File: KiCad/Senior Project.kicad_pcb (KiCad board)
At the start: 4 copper layers, 59.2 x 89.2 mm, 46 parts, among them J2 Screw_Terminal_01x02, J3 Screw_Terminal_01x06, J4 Conn_ARM_JTAG_SWD_10, J5 Conn_01x03, J6 Conn_01x02, J7 USB4105-GF-A, Q2 IRLML0030, Q3 IRLML0030, Q4 IRLML0030, SW1 SW_Push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

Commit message: all DRC error fixed other than hole clearence issue, Only radio connection left to route
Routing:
- net GND: track 34.4 -> 7.33 mm, vias 4 -> 10
- net +3V3: track 216.8 -> 222.3 mm
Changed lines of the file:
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@@
-	)
-	(segment
-		(start 166.2 124.9)
-		(end 169 122.1)
-		(width 0.2)
-		(layer "F.Cu")
-		(net 1)
 	)
 	(segment
@@
 	)
 	(segment
-		(start 169 135.3)
-		(end 166.2 132.5)
-		(width 0.2)
-		(layer "F.Cu")
-		(net 1)
-	)
-	(segment
-		(start 166.2 125.125)
-		(end 163.945 125.125)
-		(width 0.2)
-		(layer "F.Cu")
-		(net 1)
-	)
-	(segment
 		(start 174.7 135.3)
 		(end 176.6 135.3)
@@
 	)
 	(segment
-		(start 156.860589 109.258217)
-		(end 155.284653 107.682281)
-		(width 0.2)
-		(layer "F.Cu")
-		(net 1)
-	)
-	(segment
 		(start 140.5 93.2)
 		(end 140.5 92.7)
@@
 		(start 163.945 125.125)
 		(end 163.6 125.47)
-		(width 0.2)
-		(layer "F.Cu")
-		(net 1)
-	)
-	(segment
-		(start 179.4 124.9)
-		(end 176.6 122.1)
 		(width 0.2)
 		(layer "F.Cu")
@@
 	)
 	(segment
-		(start 179.4 132.5)
-		(end 176.6 135.3)
-		(width 0.2)
-		(layer "F.Cu")
-		(net 1)
-	)
-	(segment
 		(start 145.7 123.545)
 		(end 145.7 122.9)
@@
 	)
 	(segment
-		(start 160.260589 111.339411)
-		(end 157.860589 111.339411)
-		(width 0.2)
-		(layer "F.Cu")
-		(net 1)
-	)
-	(segment
 		(start 147.6 123.4)
 		(end 147.8413 123.4)
@@
 	)
 	(segment
-		(start 156.860589 110.239411)
-		(end 156.860589 109.258217)
-		(width 0.2)
-		(layer "F.Cu")
-		(net 1)
-	)
-	(segment
 		(start 147.455 123.545)
 		(end 147.6 123.4)
-		(width 0.2)
-		(layer "F.Cu")
-		(net 1)
-	)
-	(segment
-		(start 159.460589 109.939411)
-		(end 160.560589 111.039411)
-		(width 0.2)
-		(layer "F.Cu")
-		(net 1)
-	)
-	(segment
-		(start 157.860589 111.239411)
-		(end 156.860589 110.239411)
-		(width 0.2)
-		(layer "F.Cu")
-		(net 1)
-	)
-	(segment
-		(start 160.560589 111.039411)
-		(end 160.260589 111.339411)
 		(width 0.2)
 		(layer "F.Cu")
@@
 	)
 	(via
+		(at 149.2 119.3)
+		(size 0.6)
+		(drill 0.3)
+		(layers "F.Cu" "B.Cu")
+		(free yes)
+		(net 1)
+	)
+	(via
 		(at 142.55 124.25)
 		(size 0.6)
@@
 	)
 	(via
+		(at 163.2 105.45)
+		(size 0.6)
+		(drill 0.3)
+		(layers "F.Cu" "B.Cu")
+		(free yes)
+		(net 1)
+	)
+	(via
+		(at 148.95 76)
+		(size 0.6)
+		(drill 0.3)
+		(layers "F.Cu" "B.Cu")
+		(free yes)
+		(net 1)
+	)
+	(via
 		(at 145.7 122.9)
 		(size 0.6)
@@
 		(drill 0.3)
 		(layers "F.Cu" "B.Cu")
+		(net 1)
+	)
+	(via
+		(at 159.45 111.35)
+		(size 0.6)
+		(drill 0.3)
+		(layers "F.Cu" "B.Cu")
+		(free yes)
+		(net 1)
+	)
+	(via
+		(at 148.25 71.2)
+		(size 0.6)
+		(drill 0.3)
+		(layers "F.Cu" "B.Cu")
+		(free yes)
+		(net 1)
+	)
+	(via
+		(at 151.4 70.75)
+		(size 0.6)
+		(drill 0.3)
+		(layers "F.Cu" "B.Cu")
+		(free yes)
 		(net 1)
 	)
@@
 	)
 	(segment
-		(start 139.152812 108.785616)
-		(end 139.838428 108.1)
-		(width 0.300387)
-		(layer "F.Cu")
-		(net 2)
-	)
-	(segment
 		(start 156.182679 106.784256)
 		(end 156.184256 106.784256)
@@
 	)
 	(segment
+		(start 143.05 108.788428)
+		(end 142.361572 108.1)
+		(width 0.300387)
+		(layer "F.Cu")
+		(net 2)
+	)
+	(segment
 		(start 170.1 98.05)
 		(end 170.1 98.013044)
@@
 	)
 	(segment
+		(start 142.361572 108.1)
+		(end 141.1 108.1)
+		(width 0.300387)
+		(layer "F.Cu")
+		(net 2)
+	)
+	(segment
 		(start 147.65 124.65)
 		(end 148.45 125.45)
@@
 	)
 	(segment
+		(start 138.40145 111.048344)
+		(end 143.001656 111.048344)
+		(width 0.300387)
+		(layer "F.Cu")
+		(net 2)
+	)
+	(segment
 		(start 143.4 111.35)
 		(end 143.4 108.1)
@@
 	)
 	(segment
-		(start 139.152812 110.79855)
-		(end 139.152812 108.785616)
-		(width 0.300387)
-		(layer "F.Cu")
-		(net 2)
-	)
-	(segment
 		(start 141.2 78.990718)
 		(end 137.95 82.240718)
@@
 	)
 	(segment
-		(start 137.8 110.79855)
-		(end 139.152812 110.79855)
-		(width 0.300387)
-		(layer "F.Cu")
-		(net 2)
-	)
-	(segment
 		(start 145.02 118.793174)
 		(end 145.181587 118.631587)
@@
 	)
 	(segment
+		(start 143.001656 111.048344)
+		(end 143.05 111)
+		(width 0.300387)
+		(layer "F.Cu")
+		(net 2)
+	)
+	(segment
 		(start 170 99.188044)
 		(end 169.838044 99.35)
@@
 	)
 	(segment
+		(start 138.151656 110.79855)
+		(end 138.40145 111.048344)
+		(width 0.300387)
+		(layer "F.Cu")
+		(net 2)
+	)
+	(segment
 		(start 139.4 111.35)
 		(end 143.4 111.35)
@@
 	)
 	(segment
+		(start 143.05 111)
+		(end 143.05 108.788428)
+		(width 0.300387)
+		(layer "F.Cu")
+		(net 2)
+	)
+	(segment
 		(start 162.909727 107.140273)
 		(end 162.609727 107.140273)
@@
 		(layer "F.Cu")
 		(net 2)
+	)
+	(segment
+		(start 137.8 110.79855)
+		(end 138.151656 110.79855)
+		(width 0.300387)
+		(layer "F.Cu")
+		(net 2)

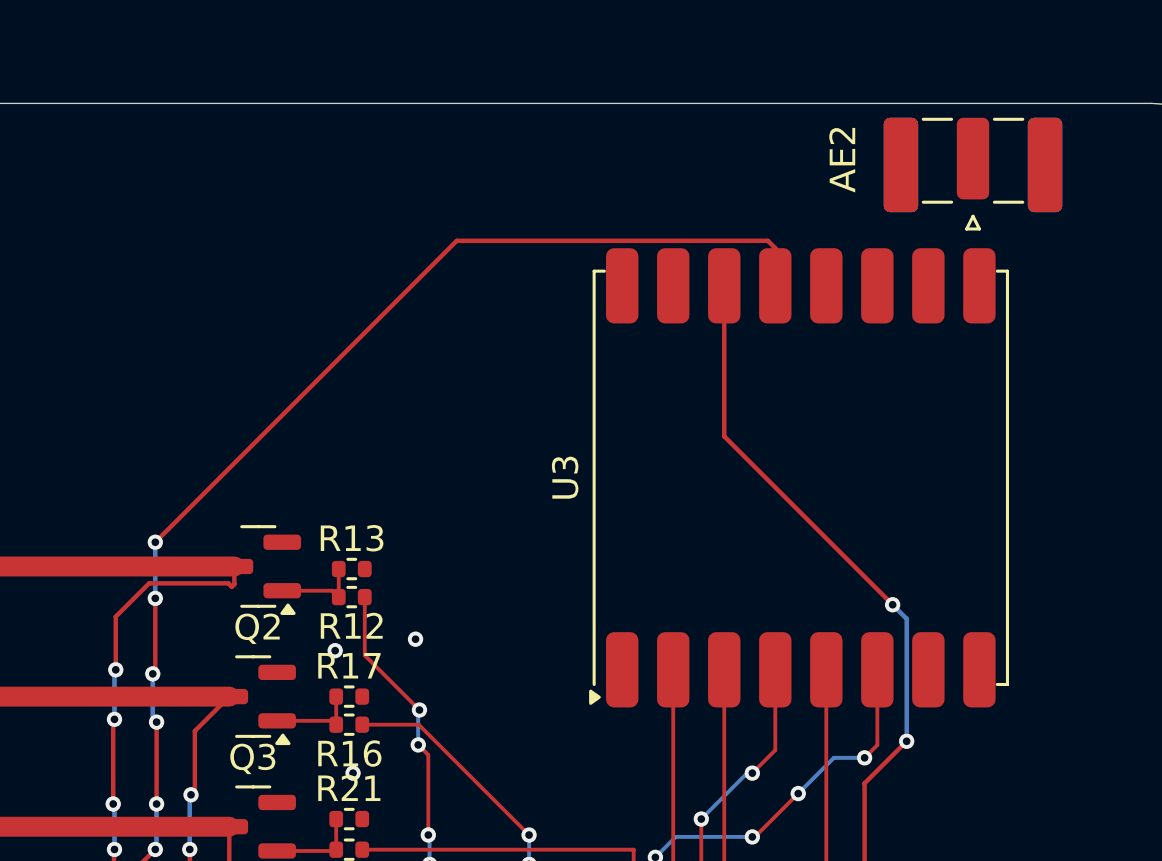
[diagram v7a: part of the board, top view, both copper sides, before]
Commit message: all DRC error fixed other than hole clearence issue, Only radio connection left to route v2
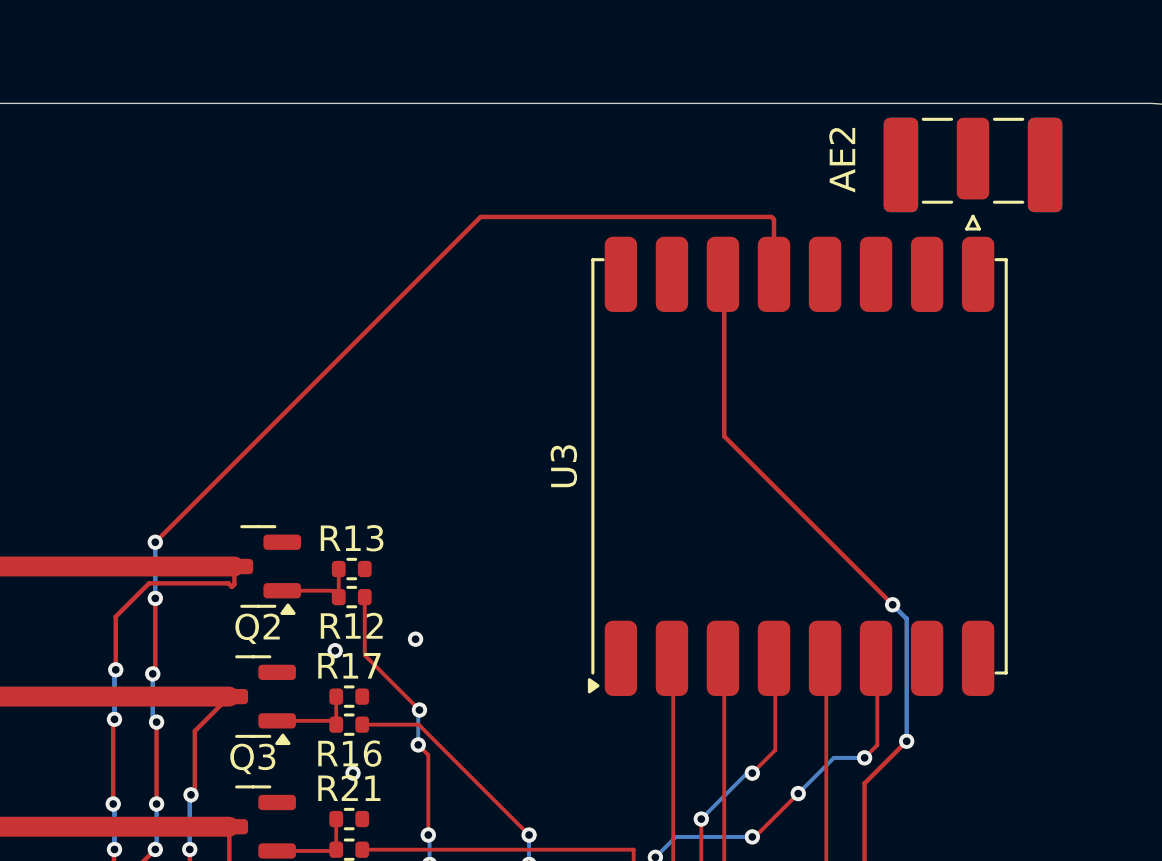
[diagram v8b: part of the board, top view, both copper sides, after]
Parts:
- moved U3 0.45 mm to (166.4, 64.0)
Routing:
- net +3V3: track 222.3 -> 225.1 mm
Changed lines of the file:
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@@
 	(footprint "RF_Module:HOPERF_RFM9XW_SMD"
 		(layer "F.Cu")
-		(at 166.5 64.425 90)
+		(at 166.45 63.975 90)
 		(descr "Low Power Long Range Transceiver Module SMD-16 (https://www.hoperf.com/data/upload/portal/20181127/5bfcbea20e9ef.pdf)")
 		(tags "LoRa Low Power Long Range Transceiver Module")
@@
 	)
 	(segment
+		(start 165.35 54.2)
+		(end 165.45 54.3)
+		(width 0.175)
+		(layer "F.Cu")
+		(net 2)
+	)
+	(segment
 		(start 144.775001 119.475)
 		(end 145.02 119.475)
@@
 	)
 	(segment
+		(start 153.95 54.2)
+		(end 165.35 54.2)
+		(width 0.175)
+		(layer "F.Cu")
+		(net 2)
+	)
+	(segment
 		(start 144.18 124.275)
 		(end 144.18 122.8425)
@@
 	)
 	(segment
+		(start 141.2 66.95)
+		(end 153.95 54.2)
+		(width 0.175)
+		(layer "F.Cu")
+		(net 2)
+	)
+	(segment
 		(start 147.65 124.65)
 		(end 148.45 125.45)
@@
 	)
 	(segment
-		(start 165.2115 55.1365)
-		(end 153.0135 55.1365)
-		(width 0.175)
-		(layer "F.Cu")
-		(net 2)
-	)
-	(segment
 		(start 141.5 124.3)
 		(end 142.0735 124.8735)
@@
 	)
 	(segment
-		(start 153.0135 55.1365)
-		(end 141.2 66.95)
-		(width 0.175)
-		(layer "F.Cu")
-		(net 2)
-	)
-	(segment
 		(start 145.47 124.275)
 		(end 145.7 124.505)
@@
 	)
 	(segment
+		(start 165.45 54.3)
+		(end 165.45 56.45)
+		(width 0.175)
+		(layer "F.Cu")
+		(net 2)
+	)
+	(segment
 		(start 145.02 120.02)
 		(end 145.9 120.9)
@@
 	)
 	(segment
+		(start 173.5 52.1625)
+		(end 173.25 51.9125)
+		(width 0.431556)
+		(layer "F.Cu")
+		(net 29)
+	)
+	(segment
